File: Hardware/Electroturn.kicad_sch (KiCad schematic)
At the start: 27 parts, among them J1 Encoder Terminal, J2 Stepper Motor Terminal, U1 Teensy 4.0

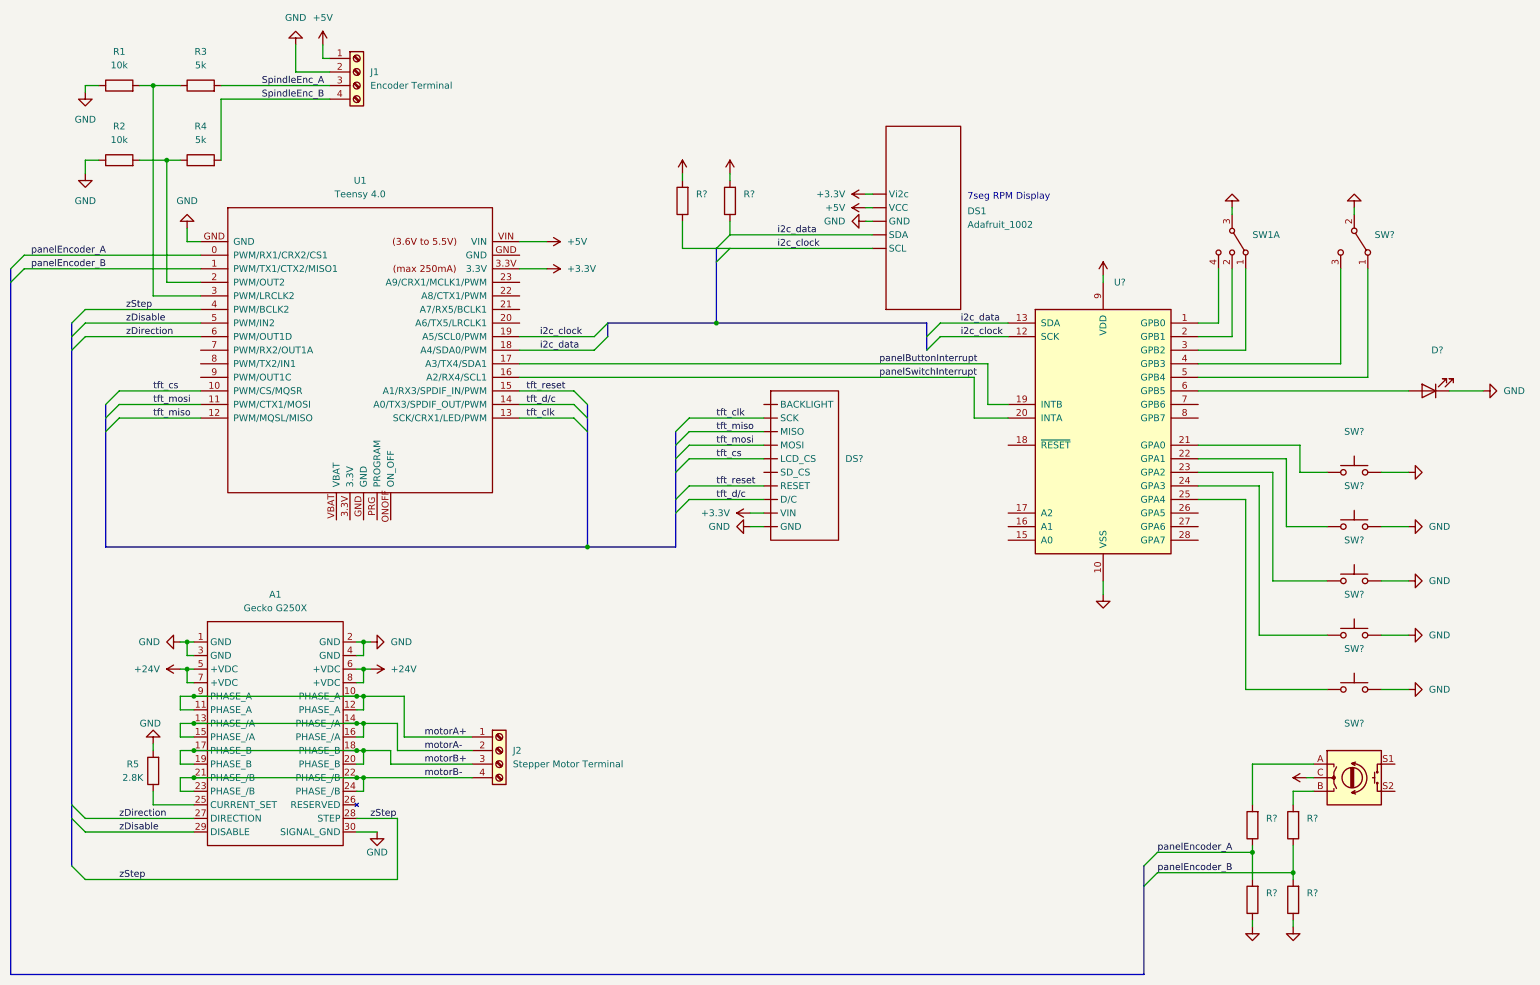
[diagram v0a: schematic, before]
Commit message: Fixing mislabeled interrupt pins
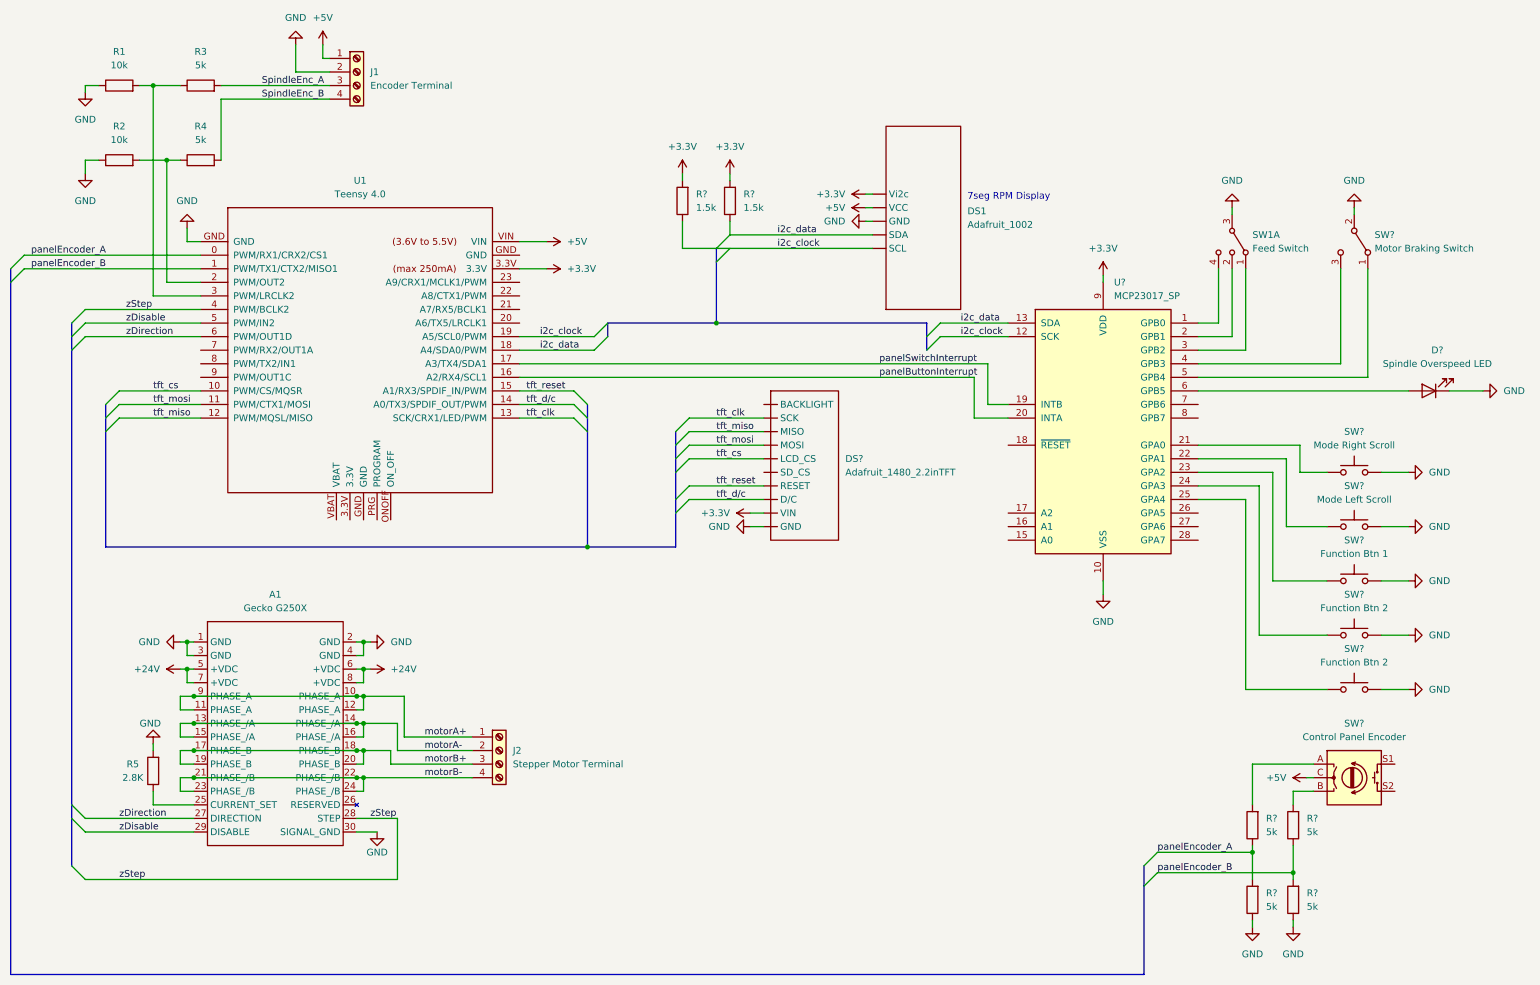
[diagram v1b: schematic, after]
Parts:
- D?: value (none) -> Spindle Overspeed LED
- DS?: value (none) -> Adafruit_1480_2.2inTFT
- R? (x4): value (none) -> 5k
- R? (x2): value (none) -> 1.5k
- SW1: value (none) -> Feed Switch
- SW?: value (none) -> Mode Right Scroll
- SW?: value (none) -> Function Btn 1
- SW?: value (none) -> Mode Left Scroll
- SW? (x2): value (none) -> Function Btn 2
- SW?: value (none) -> Motor Braking Switch
- SW?: value (none) -> Control Panel Encoder
- U?: value (none) -> MCP23017_SP; footprint (none) -> Package_DIP:DIP-28_W7.62mm
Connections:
- net panelButtonInterrupt: now also U1.16 (A2/RX4/SCL1), U?.20 (INTA); no longer U1.17 (A3/TX4/SDA1), U?.19 (INTB)
- net panelSwitchInterrupt: now also U1.17 (A3/TX4/SDA1), U?.19 (INTB); no longer U1.16 (A2/RX4/SCL1), U?.20 (INTA)
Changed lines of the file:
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@@
     (effects (font (size 1.27 1.27)) (justify left bottom))
   )
-  (label "panelSwitchInterrupt" (at 214.63 99.06 0)
+  (label "panelButtonInterrupt" (at 214.63 99.06 0)
     (effects (font (size 1.27 1.27)) (justify left bottom))
   )
@@
     (effects (font (size 1.27 1.27)) (justify left bottom))
   )
-  (label "panelButtonInterrupt" (at 214.63 96.52 0)
+  (label "panelSwitchInterrupt" (at 214.63 96.52 0)
     (effects (font (size 1.27 1.27)) (justify left bottom))
   )
@@
       (effects (font (size 1.27 1.27)) hide)
     )
-    (property "Value" "" (id 1) (at 186.69 55.88 0))
+    (property "Value" "+3.3V" (id 1) (at 186.69 55.88 0))
     (property "Footprint" "" (id 2) (at 186.69 60.96 0)
       (effects (font (size 1.27 1.27)) hide)
@@
     (in_bom yes) (on_board yes) (fields_autoplaced)
     (property "Reference" "SW?" (id 0) (at 303.53 109.22 0))
-    (property "Value" "" (id 1) (at 303.53 111.76 0))
+    (property "Value" "Mode Right Scroll" (id 1) (at 303.53 111.76 0))
     (property "Footprint" "" (id 2) (at 303.53 111.76 0)
       (effects (font (size 1.27 1.27)) hide)
@@
       (effects (font (size 1.27 1.27)) (justify right))
     )
-    (property "Value" "" (id 1) (at 287.02 184.1499 0)
+    (property "Value" "5k" (id 1) (at 287.02 184.1499 0)
       (effects (font (size 1.27 1.27)) (justify right))
     )
@@
     (in_bom yes) (on_board yes) (fields_autoplaced)
     (property "Reference" "SW?" (id 0) (at 303.53 129.54 0))
-    (property "Value" "" (id 1) (at 303.53 132.08 0))
+    (property "Value" "Function Btn 1" (id 1) (at 303.53 132.08 0))
     (property "Footprint" "" (id 2) (at 303.53 132.08 0)
       (effects (font (size 1.27 1.27)) hide)
@@
       (effects (font (size 1.27 1.27)) hide)
     )
-    (property "Value" "" (id 1) (at 284.48 207.01 0))
+    (property "Value" "GND" (id 1) (at 284.48 207.01 0))
     (property "Footprint" "" (id 2) (at 284.48 201.93 0)
       (effects (font (size 1.27 1.27)) hide)
@@
     (in_bom yes) (on_board yes) (fields_autoplaced)
     (property "Reference" "SW?" (id 0) (at 303.53 119.38 0))
-    (property "Value" "" (id 1) (at 303.53 121.92 0))
+    (property "Value" "Mode Left Scroll" (id 1) (at 303.53 121.92 0))
     (property "Footprint" "" (id 2) (at 303.53 121.92 0)
       (effects (font (size 1.27 1.27)) hide)
@@
       (effects (font (size 1.27 1.27)) (justify right))
     )
-    (property "Value" "" (id 1) (at 294.64 198.1199 0)
+    (property "Value" "5k" (id 1) (at 294.64 198.1199 0)
       (effects (font (size 1.27 1.27)) (justify right))
     )
@@
       (effects (font (size 1.27 1.27)) hide)
     )
-    (property "Value" "" (id 1) (at 280.67 62.23 0))
+    (property "Value" "GND" (id 1) (at 280.67 62.23 0))
     (property "Footprint" "" (id 2) (at 280.67 67.31 0)
       (effects (font (size 1.27 1.27)) hide)
@@
     (in_bom yes) (on_board yes) (fields_autoplaced)
     (property "Reference" "SW?" (id 0) (at 303.53 139.7 0))
-    (property "Value" "" (id 1) (at 303.53 142.24 0))
+    (property "Value" "Function Btn 2" (id 1) (at 303.53 142.24 0))
     (property "Footprint" "" (id 2) (at 303.53 142.24 0)
       (effects (font (size 1.27 1.27)) hide)
@@
       (effects (font (size 1.27 1.27)) (justify left))
     )
-    (property "Value" "" (id 1) (at 307.34 74.9299 90)
+    (property "Value" "Motor Braking Switch" (id 1) (at 307.34 74.9299 90)
       (effects (font (size 1.27 1.27)) (justify left))
     )
@@
       (effects (font (size 1.27 1.27)) (justify left))
     )
-    (property "Value" "" (id 1) (at 208.28 116.8399 0)
+    (property "Value" "Adafruit_1480_2.2inTFT" (id 1) (at 208.28 116.8399 0)
       (effects (font (size 1.27 1.27)) (justify left))
     )
@@
     (in_bom yes) (on_board yes) (fields_autoplaced)
     (property "Reference" "SW?" (id 0) (at 303.53 163.83 0))
-    (property "Value" "" (id 1) (at 303.53 166.37 0))
+    (property "Value" "Control Panel Encoder" (id 1) (at 303.53 166.37 0))
     (property "Footprint" "" (id 2) (at 299.72 169.926 0)
       (effects (font (size 1.27 1.27)) hide)
@@
       (effects (font (size 1.27 1.27)) (justify right))
     )
-    (property "Value" "" (id 1) (at 189.23 67.3099 0)
+    (property "Value" "1.5k" (id 1) (at 189.23 67.3099 0)
       (effects (font (size 1.27 1.27)) (justify right))
     )
@@
       (effects (font (size 1.27 1.27)) (justify left))
     )
-    (property "Value" "" (id 1) (at 258.5594 83.82 0)
-      (effects (font (size 1.27 1.27)) (justify left))
-    )
-    (property "Footprint" "" (id 2) (at 261.62 134.62 0)
+    (property "Value" "MCP23017_SP" (id 1) (at 258.5594 83.82 0)
+      (effects (font (size 1.27 1.27)) (justify left))
+    )
+    (property "Footprint" "Package_DIP:DIP-28_W7.62mm" (id 2) (at 261.62 134.62 0)
       (effects (font (size 1.27 1.27)) (justify left) hide)
     )
@@
       (effects (font (size 1.27 1.27)) (justify right))
     )
-    (property "Value" "" (id 1) (at 294.64 184.1499 0)
+    (property "Value" "5k" (id 1) (at 294.64 184.1499 0)
       (effects (font (size 1.27 1.27)) (justify right))
     )
@@
       (effects (font (size 1.27 1.27)) (justify right))
     )
-    (property "Value" "" (id 1) (at 287.02 198.1199 0)
+    (property "Value" "5k" (id 1) (at 287.02 198.1199 0)
       (effects (font (size 1.27 1.27)) (justify right))
     )
@@
       (effects (font (size 1.27 1.27)) hide)
     )
-    (property "Value" "" (id 1) (at 317.5 116.8399 90)
+    (property "Value" "GND" (id 1) (at 317.5 116.8399 90)
       (effects (font (size 1.27 1.27)) (justify right))
     )
@@
       (effects (font (size 1.27 1.27)) hide)
     )
-    (property "Value" "" (id 1) (at 177.8 55.88 0))
+    (property "Value" "+3.3V" (id 1) (at 177.8 55.88 0))
     (property "Footprint" "" (id 2) (at 177.8 60.96 0)
       (effects (font (size 1.27 1.27)) hide)
@@
     (in_bom yes) (on_board yes) (fields_autoplaced)
     (property "Reference" "SW?" (id 0) (at 303.53 149.86 0))
-    (property "Value" "" (id 1) (at 303.53 152.4 0))
+    (property "Value" "Function Btn 2" (id 1) (at 303.53 152.4 0))
     (property "Footprint" "" (id 2) (at 303.53 152.4 0)
       (effects (font (size 1.27 1.27)) hide)
@@
       (effects (font (size 1.27 1.27)) hide)
     )
-    (property "Value" "" (id 1) (at 303.53 62.23 0))
+    (property "Value" "GND" (id 1) (at 303.53 62.23 0))
     (property "Footprint" "" (id 2) (at 303.53 67.31 0)
       (effects (font (size 1.27 1.27)) hide)
@@
       (effects (font (size 1.27 1.27)) (justify left))
     )
-    (property "Value" "" (id 1) (at 284.48 74.9299 90)
+    (property "Value" "Feed Switch" (id 1) (at 284.48 74.9299 90)
       (effects (font (size 1.27 1.27)) (justify left))
     )
@@
     (pin "3")
     (pin "4")
-    (pin "5")
-    (pin "6")
-    (pin "7")
-    (pin "8")
   )
   (symbol (lib_id "power:GND") (at 66.04 45.72 0) (unit 1)
@@
       (effects (font (size 1.27 1.27)) hide)
     )
-    (property "Value" "" (id 1) (at 290.83 173.9899 90)
+    (property "Value" "+5V" (id 1) (at 290.83 173.9899 90)
       (effects (font (size 1.27 1.27)) (justify left))
     )
@@
       (effects (font (size 1.27 1.27)) (justify right))
     )
-    (property "Value" "" (id 1) (at 180.34 67.3099 0)
+    (property "Value" "1.5k" (id 1) (at 180.34 67.3099 0)
       (effects (font (size 1.27 1.27)) (justify right))
     )
@@
       (effects (font (size 1.27 1.27)) hide)
     )
-    (property "Value" "" (id 1) (at 256.54 74.93 0))
+    (property "Value" "+3.3V" (id 1) (at 256.54 74.93 0))
     (property "Footprint" "" (id 2) (at 256.54 80.01 0)
       (effects (font (size 1.27 1.27)) hide)
@@
       (effects (font (size 1.27 1.27)) hide)
     )
-    (property "Value" "" (id 1) (at 256.54 144.78 0))
+    (property "Value" "GND" (id 1) (at 256.54 144.78 0))
     (property "Footprint" "" (id 2) (at 256.54 139.7 0)
       (effects (font (size 1.27 1.27)) hide)
@@
     (in_bom yes) (on_board yes) (fields_autoplaced)
     (property "Reference" "D?" (id 0) (at 319.0875 93.98 0))
-    (property "Value" "" (id 1) (at 319.0875 96.52 0))
+    (property "Value" "Spindle Overspeed LED" (id 1) (at 319.0875 96.52 0))
     (property "Footprint" "" (id 2) (at 317.5 101.6 0)
       (effects (font (size 1.27 1.27)) hide)
@@
       (effects (font (size 1.27 1.27)) hide)
     )
-    (property "Value" "" (id 1) (at 292.1 207.01 0))
+    (property "Value" "GND" (id 1) (at 292.1 207.01 0))
     (property "Footprint" "" (id 2) (at 292.1 201.93 0)
       (effects (font (size 1.27 1.27)) hide)

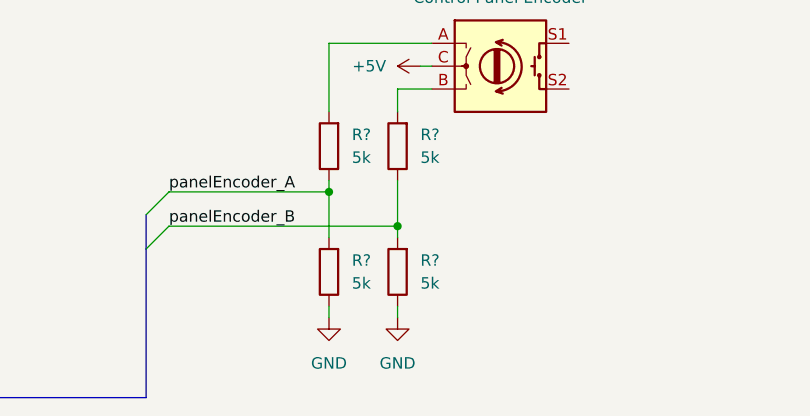
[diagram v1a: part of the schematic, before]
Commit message: Fixing R values in panel encoder voltage divider
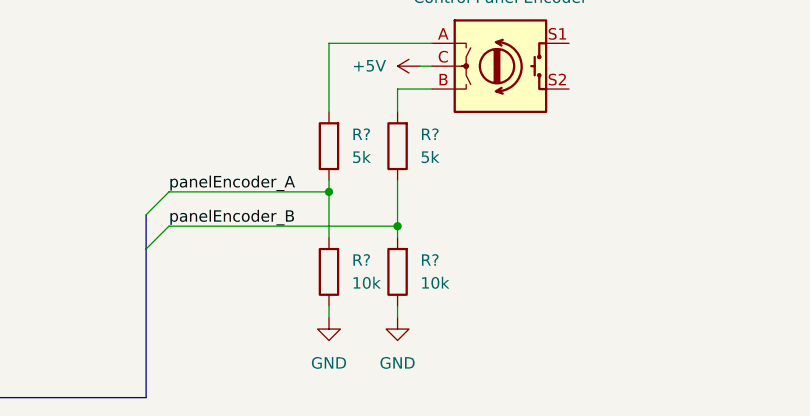
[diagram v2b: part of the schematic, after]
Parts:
- R? (x2): value 5k -> 10k
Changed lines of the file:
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@@
       (effects (font (size 1.27 1.27)) (justify right))
     )
-    (property "Value" "5k" (id 1) (at 294.64 198.1199 0)
+    (property "Value" "10k" (id 1) (at 294.64 198.1199 0)
       (effects (font (size 1.27 1.27)) (justify right))
     )
@@
       (effects (font (size 1.27 1.27)) (justify right))
     )
-    (property "Value" "5k" (id 1) (at 287.02 198.1199 0)
+    (property "Value" "10k" (id 1) (at 287.02 198.1199 0)
       (effects (font (size 1.27 1.27)) (justify right))
     )
@@
     )
     (path "/44d05f95-c05f-4d27-b008-026605ef30bf"
-      (reference "R?") (unit 1) (value "5k") (footprint "")
+      (reference "R?") (unit 1) (value "10k") (footprint "")
     )
     (path "/645e3d78-a90d-414c-aad0-e3317ada2110"
@@
     )
     (path "/8a8afa01-3935-4cd5-98f5-8932bae63ccd"
-      (reference "R?") (unit 1) (value "5k") (footprint "")
+      (reference "R?") (unit 1) (value "10k") (footprint "")
     )
     (path "/d798ac97-4344-4dfa-8632-bb28b6283358"

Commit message: Reorganizing KiCAD repo, fixing path issues
I tidied up the folder structure, and also went in and relinked all the footprints/symbols using the correct new paths. Should work across any system now. Also linked the appropriate 3D models for the Teensy and Gecko.
I updated the PCB to include all these new changes from the footprints/schematic, and in doing so it pretty much destroyed what Karson had...sorry Karson
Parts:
- gave numbers to parts that had none: 16

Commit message: Adding pin numbers to adafruit TFT symbol
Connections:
- net +3V3: now also DS2.9 (VIN); no longer DS2. (VIN)
- net GND: now also DS2.10 (GND); no longer DS2. (VIN)
- net tft_clk: now also DS2.2 (SCK); no longer DS2. (VIN)
- net tft_cs: now also DS2.5 (LCD_CS); no longer DS2. (VIN)
- net tft_d/c: now also DS2.8 (D/C); no longer DS2. (VIN)
- net tft_miso: now also DS2.3 (MISO); no longer DS2. (VIN)
- net tft_mosi: now also DS2.4 (MOSI); no longer DS2. (VIN)
- net tft_reset: now also DS2.7 (RESET); no longer DS2. (VIN)
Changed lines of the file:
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@@
+    (stroke (width 0) (type default) (color 0 0 0 0))
+  )
+  (wire (pts (xy 179.07 109.22) (xy 193.04 109.22))
     (stroke (width 0) (type default) (color 0 0 0 0))
   )
@@
     (stroke (width 0) (type default) (color 0 0 0 0))
   )
-  (wire (pts (xy 179.07 109.22) (xy 193.04 109.22))
-    (stroke (width 0) (type default) (color 0 0 0 0))
-  )
   (wire (pts (xy 123.19 171.45) (xy 138.43 171.45))
     (stroke (width 0) (type default) (color 0 0 0 0))
@@
     (stroke (width 0) (type default) (color 0 0 0 0))
   )
+  (wire (pts (xy 179.07 106.68) (xy 193.04 106.68))
+    (stroke (width 0) (type default) (color 0 0 0 0))
+  )
   (bus (pts (xy 176.53 124.46) (xy 176.53 130.81))
     (stroke (width 0) (type default) (color 0 0 0 0))
@@
     (stroke (width 0) (type default) (color 0 0 0 0))
   )
+  (wire (pts (xy 179.07 111.76) (xy 193.04 111.76))
+    (stroke (width 0) (type default) (color 0 0 0 0))
+  )
   (wire (pts (xy 118.11 168.91) (xy 123.19 168.91))
     (stroke (width 0) (type default) (color 0 0 0 0))
@@
     (stroke (width 0) (type default) (color 0 0 0 0))
   )
-  (wire (pts (xy 179.07 111.76) (xy 193.04 111.76))
-    (stroke (width 0) (type default) (color 0 0 0 0))
-  )
   (wire (pts (xy 300.99 96.52) (xy 274.32 96.52))
     (stroke (width 0) (type default) (color 0 0 0 0))
@@
   )
   (wire (pts (xy 290.83 127) (xy 290.83 114.3))
-    (stroke (width 0) (type default) (color 0 0 0 0))
-  )
-  (wire (pts (xy 179.07 106.68) (xy 193.04 106.68))
     (stroke (width 0) (type default) (color 0 0 0 0))
   )
@@
     (pin "3")
   )
-  (symbol (lib_id "Electroturn_Parts:Adafruit_1480_2.2inTFT") (at 222.25 115.57 0) (unit 1)
-    (in_bom yes) (on_board yes) (fields_autoplaced)
-    (property "Reference" "DS2" (id 0) (at 208.28 114.2999 0)
+  (symbol (lib_id "Electroturn_Parts:Adafruit_1480_2.2inTFT") (at 223.52 115.57 0) (unit 1)
+    (in_bom yes) (on_board yes) (fields_autoplaced)
+    (property "Reference" "DS2" (id 0) (at 209.55 114.2999 0)
       (effects (font (size 1.27 1.27)) (justify left))
     )
-    (property "Value" "Adafruit_1480_2.2inTFT" (id 1) (at 208.28 116.8399 0)
+    (property "Value" "Adafruit_1480_2.2inTFT" (id 1) (at 209.55 116.8399 0)
       (effects (font (size 1.27 1.27)) (justify left))
     )
-    (property "Footprint" "" (id 2) (at 208.28 134.62 0)
-      (effects (font (size 1.27 1.27)) hide)
-    )
-    (property "Datasheet" "" (id 3) (at 208.28 134.62 0)
-      (effects (font (size 1.27 1.27)) hide)
-    )
-    (pin "")
-    (pin "")
-    (pin "")
-    (pin "")
-    (pin "")
-    (pin "")
-    (pin "")
-    (pin "")
-    (pin "")
-    (pin "")
+    (property "Footprint" "" (id 2) (at 209.55 134.62 0)
+      (effects (font (size 1.27 1.27)) hide)
+    )
+    (property "Datasheet" "" (id 3) (at 209.55 134.62 0)
+      (effects (font (size 1.27 1.27)) hide)
+    )
+    (pin "1")
+    (pin "10")
+    (pin "2")
+    (pin "3")
+    (pin "4")
+    (pin "5")
+    (pin "6")
+    (pin "7")
+    (pin "8")
+    (pin "9")
   )
   (symbol (lib_id "Device:R") (at 72.39 44.45 90) (unit 1)

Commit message: More footprint work
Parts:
- removed DS1: Adafruit_1002, symbol MCU_Module:Adafruit_1002
- added DS?: Adafruit_1002_Alphanumeric, symbol Electroturn_Parts:Adafruit_1002_Alphanumeric
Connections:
- net +3V3: now also DS?.5 (Vi2c)
- net +5V: now also DS?.4 (VCC)
- net GND: now also DS?.3 (GND)
- net i2c_clock: now also DS?.1 (SCL)
- net i2c_data: now also DS?.2 (SDA)
